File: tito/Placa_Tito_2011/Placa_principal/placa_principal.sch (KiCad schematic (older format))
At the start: 28 parts, among them IC1 ATMEGA8-P, P1 CONN_2, P2 CONN_2, P3 CONN_4X2, P4 CONN_2, P5 CONN_3X2, P6 CONN_3X2, SW1 SW_PUSH_SMALL, U1 L298D, U2 REG_104-5

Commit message: Arrancamos la placa nueva
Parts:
- removed IC1: ATMEGA8-P, DIL28, symbol ATMEGA8-P
- removed P5: CONN_3X2, symbol CONN_3X2
- added C?: C, symbol C
- added C?: 220 uF, symbol CAPAPOL
- added C?: 1000 uF, symbol CAPAPOL
- added C?: 100 nF, symbol C
- added D? (x4): LED, symbol LED
- added IC?: ATMEGA88-P, DIL28, symbol ATMEGA88-P
- added K?: CONN_3, symbol CONN_3
- added P?: CONN_2, symbol CONN_2
- added R?: 10 K, symbol R
- added R? (x4): R, symbol R
- added SW?: SW_PUSH_SMALL, symbol SW_PUSH_SMALL
- C2: value 10nF -> 10 nF
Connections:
- no-connect marks 6 -> 2
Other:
- note added: "10.8 V"
- note removed: "Leds auxiliares"
- moved on the sheet: C1, P3, P4, P6, R1, R2, R3, R4, RV1, RV2, RV3, RV4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

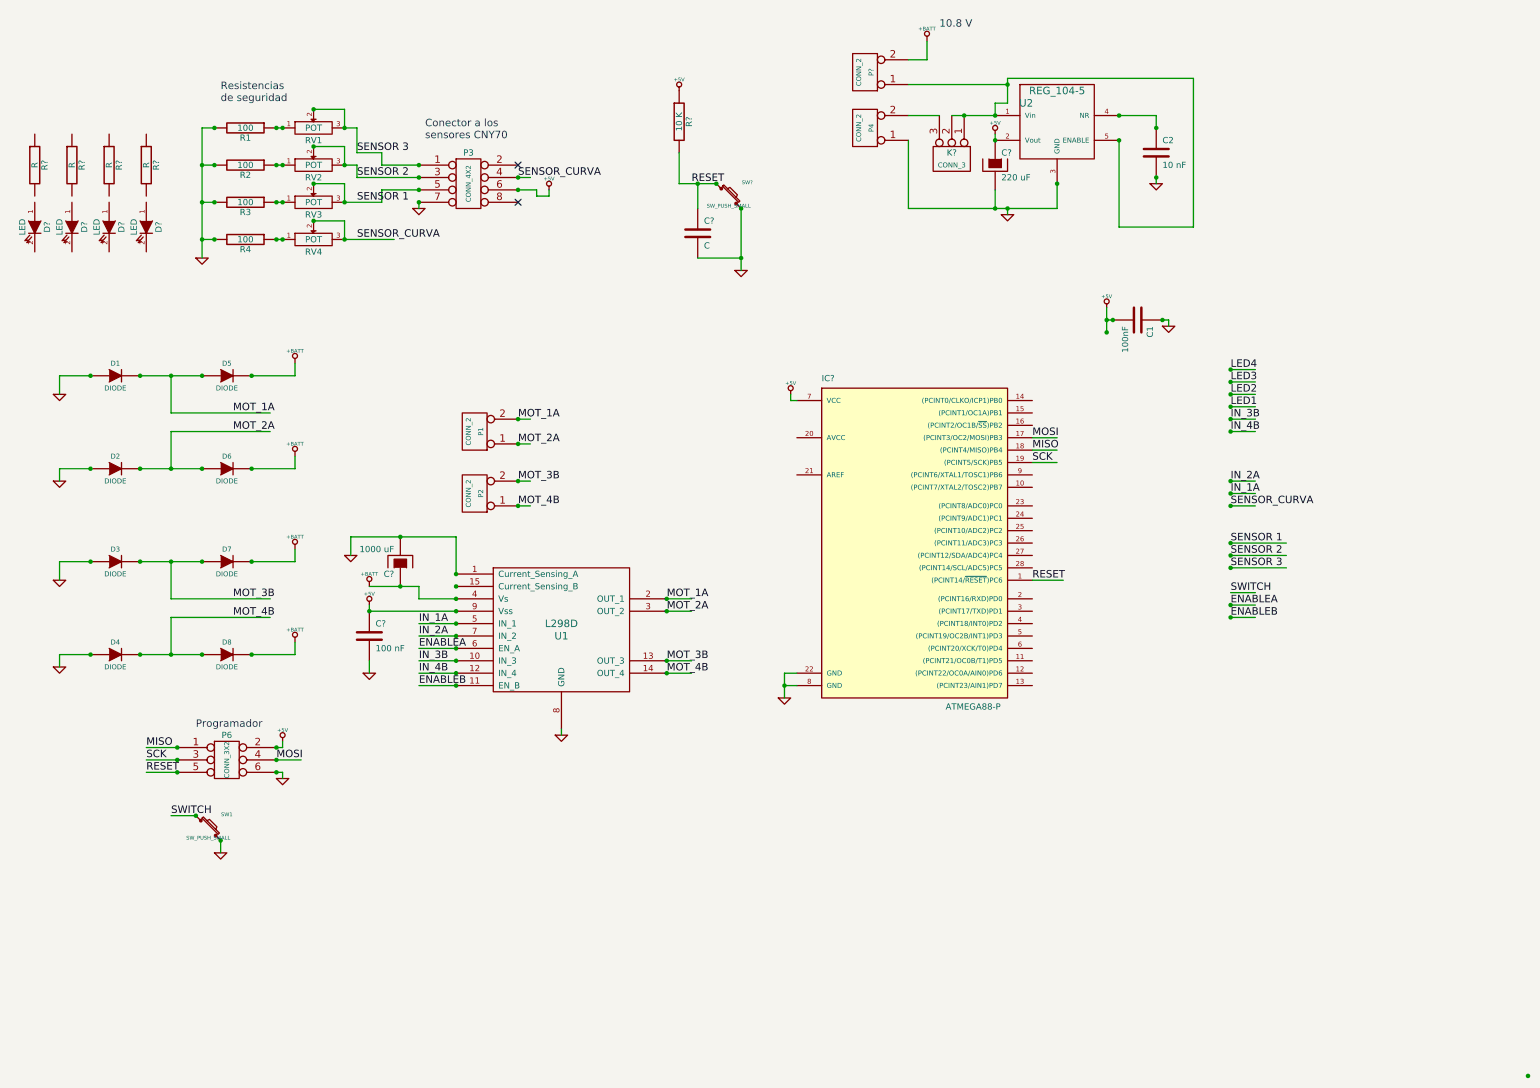
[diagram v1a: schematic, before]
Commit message: Terminamos el diseño del esquematico de la nueva placa, falta asociar componentes
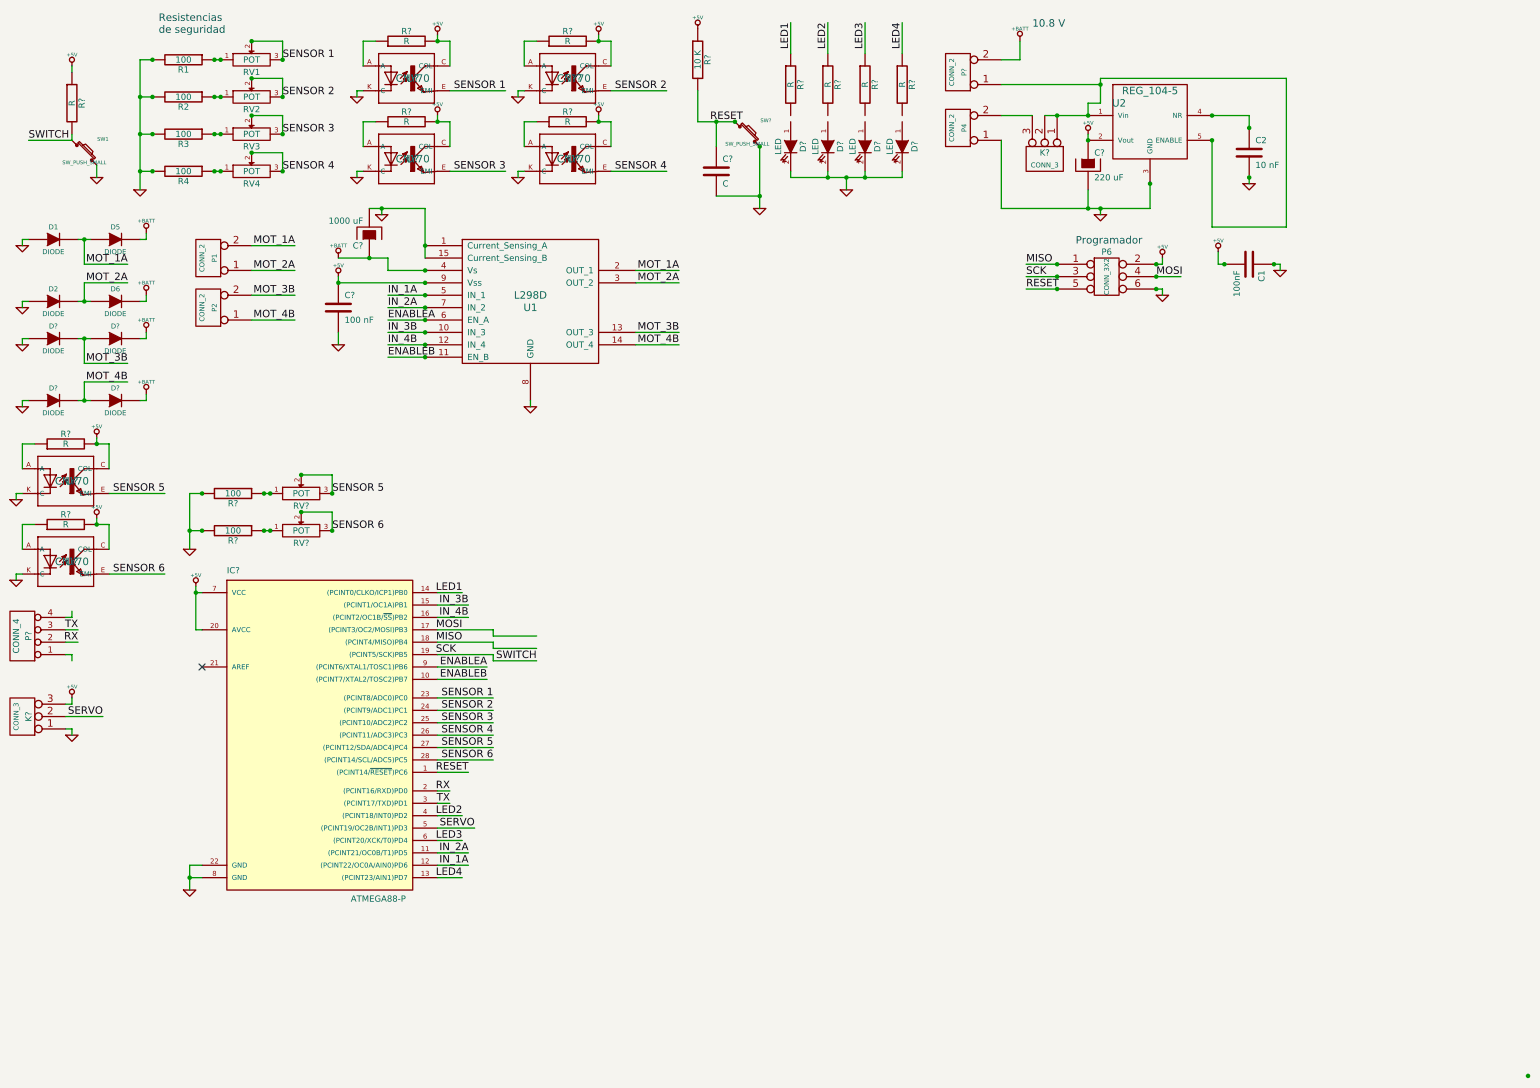
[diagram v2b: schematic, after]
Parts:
- removed D3, D4, D7, D8: DIODE, symbol DIODE
- removed P3: CONN_4X2, symbol CONN_4X2
- added ???, U? (x5): CNY70, symbol CNY70
- added D? (x4): DIODE, symbol DIODE
- added K?: CONN_3, symbol CONN_3
- added P?: CONN_4, symbol CONN_4
- added R? (x7): R, symbol R
- added R? (x2): 100, symbol R
- added RV? (x2): POT, symbol POT
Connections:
- net labels added: RX, SENSOR 4, SENSOR 5, SENSOR 6, SERVO, TX
- net labels removed: SENSOR_CURVA
- wire segments 151 -> 224
- no-connect marks 2 -> 1
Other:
- note removed: "Conector a los \nsensores CNY70"
- moved on the sheet: C1, C2, C?, D1, D2, D5, D6, D?, IC?, K?, P1, P2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

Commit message: Algunos cambios en la alimentacion del servo, y asociacion de los primeros  componentes
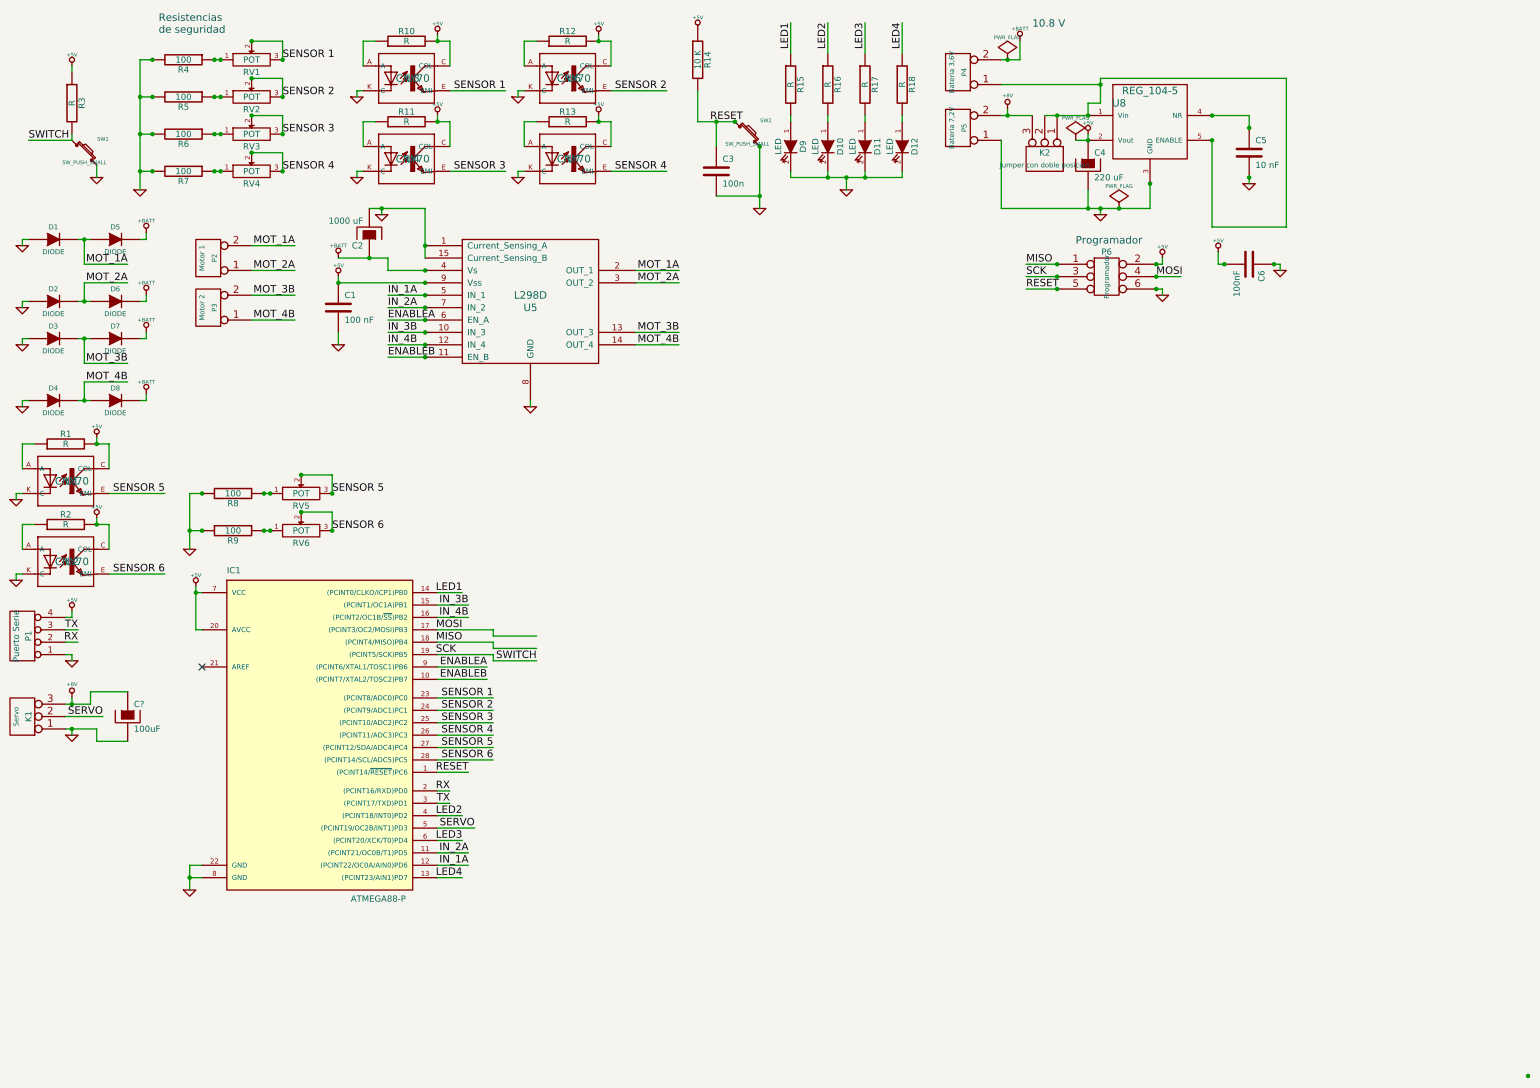
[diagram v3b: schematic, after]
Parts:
- added C?: 100uF, symbol CAPAPOL
- C3: renamed from C?; value C -> 100n
- K1: renamed from K?; value CONN_3 -> Servo
- K2: renamed from K?; value CONN_3 -> Jumper con doble posicion
- P1: renamed from P?; value CONN_4 -> Puerto Serie
- P2: renamed from P1; value CONN_2 -> Motor 1
- P3: renamed from P2; value CONN_2 -> Motor 2
- P4: renamed from P?; value CONN_2 -> Bateria 3,6V
- P5: renamed from P4; value CONN_2 -> Bateria 7,2V
- P6: value CONN_3X2 -> Programador
- gave numbers to parts that had none: 35
- renumbered C2 to C5, C1 to C6, R1 to R4, R2 to R5, R3 to R6, R4 to R7, U1 to U5, U2 to U8
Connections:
- net +5V: now also P1.4 (P4); no longer K1.3 (P3)
- net GND: now also P1.1 (P1), C?.2
- net +8V: now reaches K2.3 (P3), P5.2 (PM)
- net +8V: now also K1.3 (P3), C?.1
- net at D9.1 (A): now also R15.2
- net at D10.1 (A): now also R16.2
- net at D11.1 (A): now also R17.2
- net at D12.1 (A): now also R18.2
